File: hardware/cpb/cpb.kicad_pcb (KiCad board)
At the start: 6 copper layers, 95.9 x 90.2 mm, 238 parts, among them J1 Conn_02x20_Odd_Even, J10 SW1, J11 SW2, J12 SW3, J13 PISW1, J14 μSW1, J15 μSW2, J16 μSW3, J17 μSW4, J2 I2CExt, J3 DAC1BUF, J4 DAC2BUF, J6 Conn_02x20_Odd_Even, J7 ADC6/7, J8 ADC2/3, J9 4FBRG, J99 RBFJUMP, Q1 PMBT2222A, Q10 BSS138PS,115, Q11 BSS138PS,115, Q12 MBT2222ADW1T1, Q13 MBT2222ADW1T1, Q14 BSS138PS,115, Q15 BSS138PS,115, Q16 MBT2222ADW1T1, Q17 MBT2222ADW1T1, Q18 BSS138PS,115, Q19 BSS138PS,115, Q2 IRF9393, Q20 MBT2222ADW1T1, Q21 MBT2222ADW1T1, Q22 BSS138PS,115, Q23 BSS138PS,115, Q24 MBT2222ADW1T1, Q25 IRF7306, Q26 MBT2222ADW1T1, Q27 IRF7306, Q28 MBT2222ADW1T1, Q29 IRF7306, Q3 MBT2222ADW1T1, Q30 MBT2222ADW1T1, Q31 IRF7306, Q4 PMBT2222A, Q5 PMBT2222A, Q6 IRF9393, Q7 PMBT2222A, Q8 MBT2222ADW1T1, Q9 MBT2222ADW1T1, U1 TS912, U2 ADR420ARMZ, U3 KF33BDT, U4 STM32L072R_B-Z_Tx, U5 AP62301WU, U6 SC16IS750xBS, U7 SC18IS606, U8 KF33BDT, U9 MAX22200, Y1 14.7456MHz

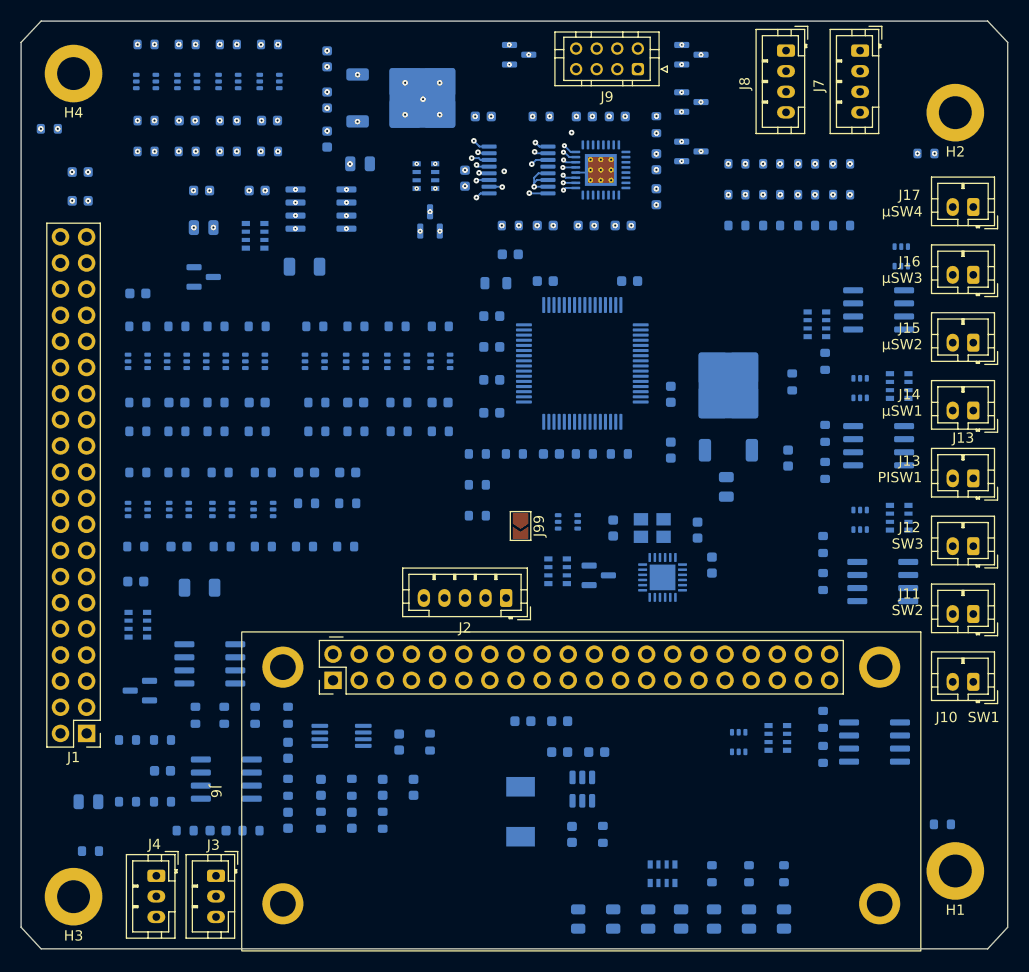
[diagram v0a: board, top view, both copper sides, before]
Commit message: cpb: continued work towards layout
- Adjust schematic; add datasheets, correct switcher output.  Additional
validation required.
- Adjust text.
- Add graphics
- Update design rules
- Perform an initial DRC in schematic & in layout.
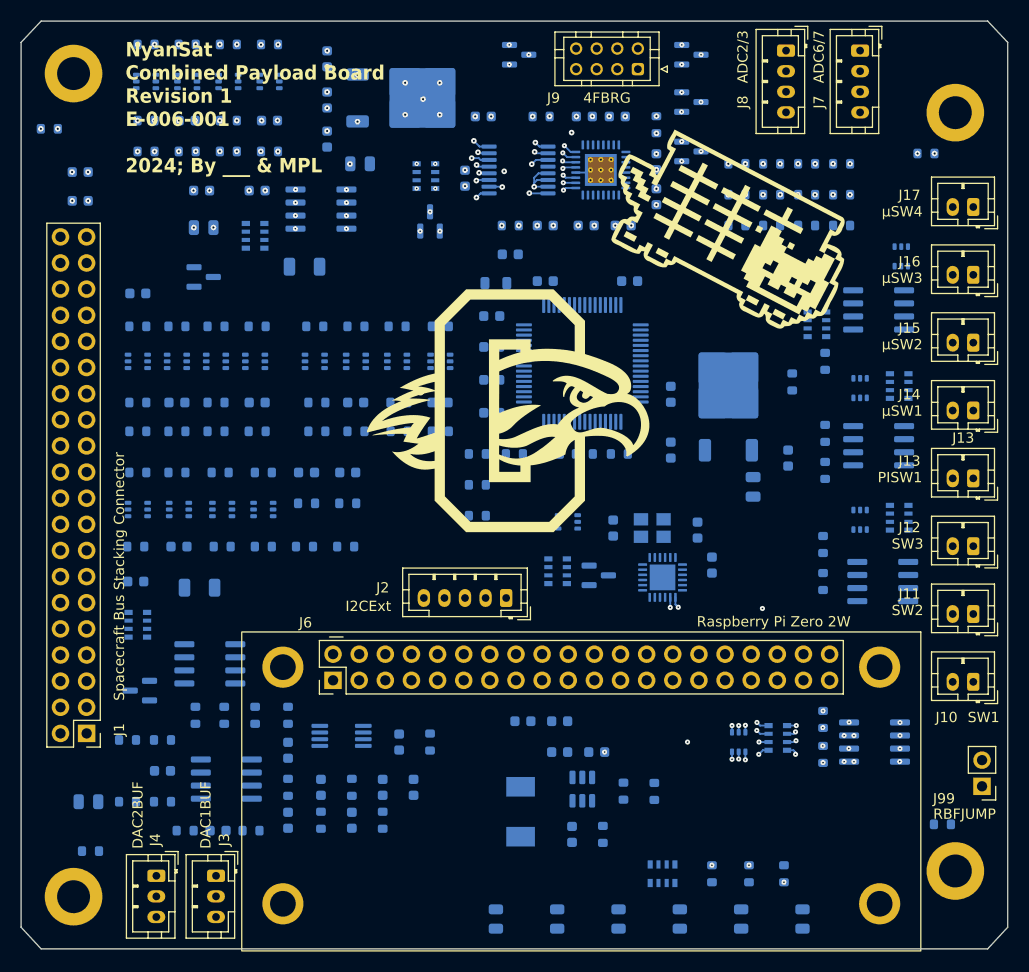
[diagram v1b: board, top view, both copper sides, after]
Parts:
- removed D4: PI3V3, LED_SMD:LED_0805_2012Metric
- added R44: 30k, Resistor_SMD:R_0603_1608Metric, B.Cu at (159.4, 133.1)
- added R45: 5.6k, Resistor_SMD:R_0603_1608Metric, B.Cu at (162.4, 133.1)
- J1: value Conn_02x20_Odd_Even -> Spacecraft Bus Stacking Connector
- J6: value Conn_02x20_Odd_Even -> Raspberry Pi Zero 2W
- J99: footprint Jumper:SolderJumper-2_P1.3mm_Open_TrianglePad1.0x1.5mm -> Connector_PinHeader_2.54mm:PinHeader_1x02_P2.54mm_Vertical
- moved J99 51.5 mm to (194.2, 132.6), turned to 180 degrees
- moved D7 8.00 mm to (147.0, 145.5)
- moved D6 5.44 mm to (153.0, 145.5)
- moved D3 3.32 mm to (164.9, 145.5)
- moved D5 2.88 mm to (158.9, 145.5)
- moved C8 2.60 mm to (172.0, 103.5)
- moved D1 1.80 mm to (176.8, 145.5)
- moved D2 0.76 mm to (170.8, 145.5)
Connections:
- RN2 pad 1: Net-(D4-A) -> (no net)
- RN2 pad 8: /PI3V3 -> (no net)
- U5 pad 4: +5V -> Net-(U5-FB)
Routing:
- net /SW2: track 0.00 -> 22.6 mm, vias 0 -> 3
- net /SW1: track 0.00 -> 21.9 mm, vias 0 -> 3
- net /PairPowerSwitches1/OUT2: track 0.00 -> 14.7 mm, vias 0 -> 2
- net Net-(Q24A-C1): track 0.00 -> 13.0 mm, vias 0 -> 3
- net Net-(Q24B-C2): track 0.00 -> 11.8 mm, vias 0 -> 3
- net /PairPowerSwitches1/OUT1: track 0.00 -> 11.6 mm, vias 0 -> 2
- net Net-(Q24B-B2): track 0.00 -> 10.2 mm, vias 0 -> 3
- net Net-(Q24A-B1): track 0.00 -> 9.43 mm, vias 0 -> 3
- net GND: track 10.4 -> 14.2 mm, vias 34 -> 38
- net +7.5V: track 0.00 -> 0.10 mm, vias 0 -> 8
- net +3.3V: track 0.00 -> 0.03 mm, vias 2 -> 3
- net +5V: vias 0 -> 1
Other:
- board text added: "NyanSat Combined Payload Board Revision 1 E-006-001 2024; By ___ & MPL"

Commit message: hardware/cpb: continuing of board layout
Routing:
- net GND: track 14.2 -> 28.9 mm, vias 38 -> 69
- net /FourFullBridges/VM: track 0.00 -> 8.35 mm, vias 12 -> 20
- net /SDA: track 0.00 -> 4.75 mm, vias 0 -> 6
- net /SCL: track 0.00 -> 3.11 mm, vias 0 -> 4
- net /UARTSDA: track 0.00 -> 2.11 mm, vias 0 -> 4
- net Net-(Q13B-B2): track 0.00 -> 2.09 mm, vias 0 -> 4
- net Net-(Q17B-B2): track 0.00 -> 1.84 mm, vias 0 -> 4
- net /uSDA: track 0.00 -> 1.82 mm, vias 0 -> 4
- net Net-(Q12B-B2): track 0.00 -> 1.69 mm, vias 0 -> 4
- net /FourFullBridges/FBRDG3V3: track 2.21 -> 3.87 mm, vias 16 -> 18
- net Net-(Q16B-B2): track 0.00 -> 1.61 mm, vias 0 -> 4
- net Net-(Q18A-G2): track 0.00 -> 1.54 mm, vias 0 -> 3
- net Net-(Q15A-G2): track 0.00 -> 1.47 mm, vias 0 -> 3
- net Net-(Q5-B): track 0.00 -> 1.47 mm, vias 0 -> 4
- net /FourFullBridges/FBRGEN: track 0.00 -> 1.43 mm, vias 1 -> 3
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
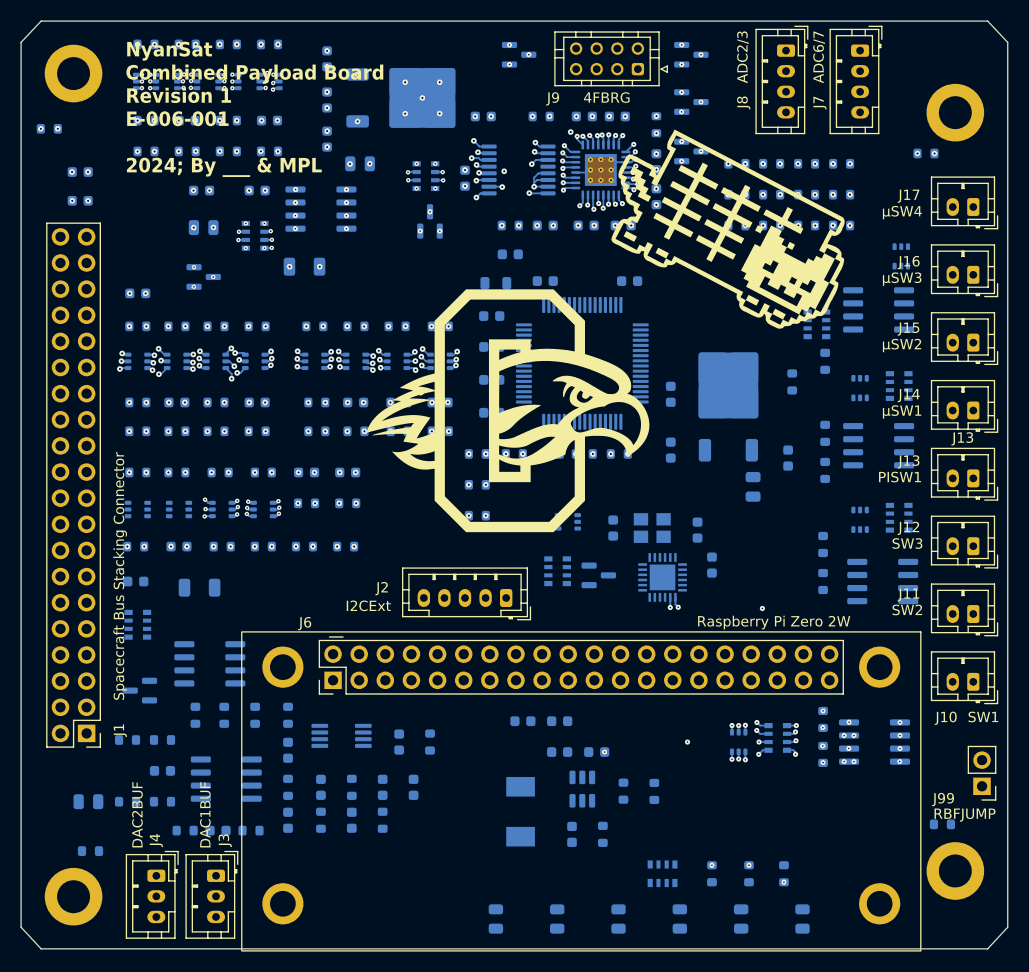
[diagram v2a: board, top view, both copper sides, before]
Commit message: hardware/cpb: Further cpb layout
Finished placing all vias and beginning of routing.
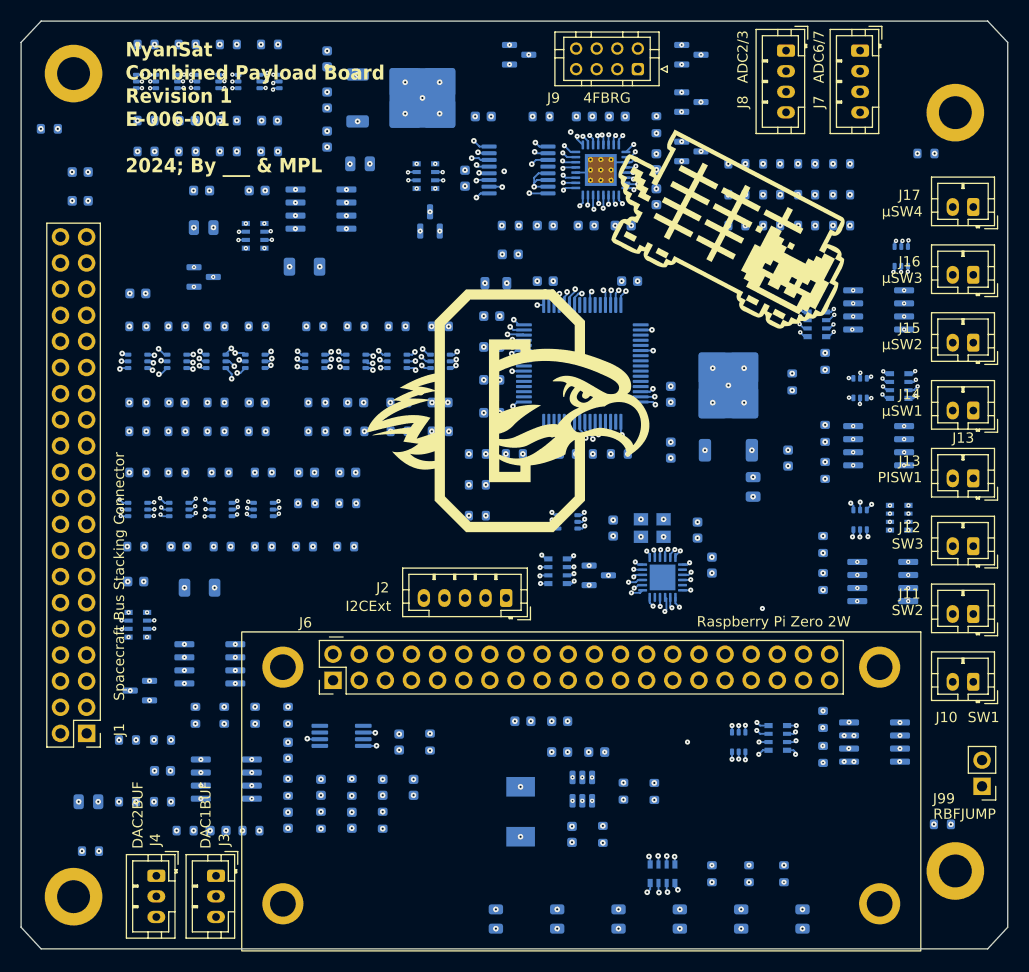
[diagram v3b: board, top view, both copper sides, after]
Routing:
- net GND: track 28.9 -> 51.2 mm, vias 69 -> 141
- net +3.3V: track 0.03 -> 11.1 mm, vias 31 -> 50
- net Net-(Q3A-C1): track 0.00 -> 3.23 mm, vias 0 -> 4
- net /uSW2: track 0.00 -> 2.82 mm, vias 0 -> 2
- net /~{MICRORST}: track 0.00 -> 2.66 mm, vias 0 -> 5
- net /uSW3: track 0.00 -> 2.62 mm, vias 0 -> 2
- net /uSW1: track 0.00 -> 2.50 mm, vias 0 -> 2
- net Net-(Q30A-B1): track 0.00 -> 2.49 mm, vias 0 -> 3
- net Net-(Q28B-B2): track 0.00 -> 2.46 mm, vias 0 -> 3
- net Net-(Q30B-B2): track 0.00 -> 2.38 mm, vias 0 -> 3
- net Net-(Q28A-B1): track 0.00 -> 2.11 mm, vias 0 -> 3
- net /TIM3_CH2: track 0.00 -> 2.06 mm, vias 0 -> 2
- net /uSW4: track 0.00 -> 2.05 mm, vias 0 -> 2
- net /GPLED: track 0.00 -> 1.81 mm, vias 0 -> 2
- net /ADC6: track 0.00 -> 1.77 mm, vias 3 -> 4
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
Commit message: cpb: routing in progress
- Adjust layout for easier routing.
- Pin swap clamping diodes to simplify routing.
- Route the high power nets
- Adjust plane pours.
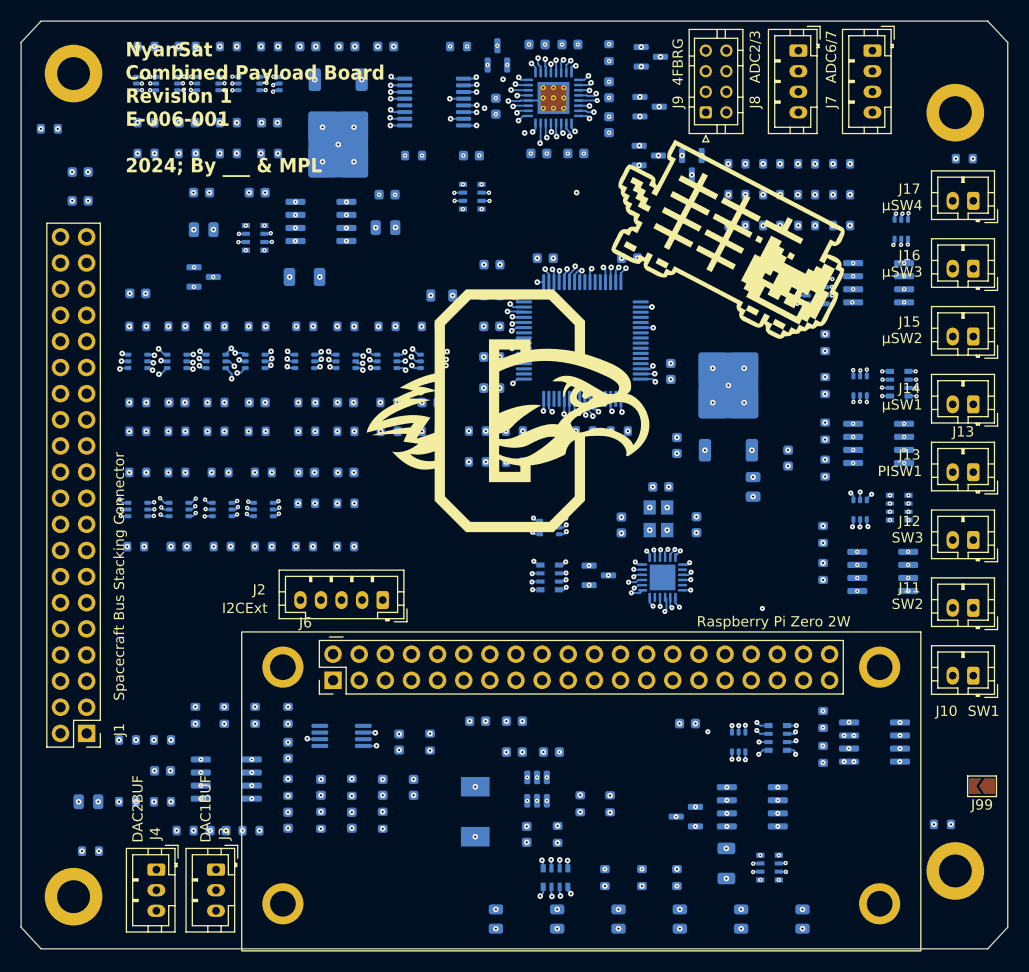
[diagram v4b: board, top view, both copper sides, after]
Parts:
- J99: footprint Connector_PinHeader_2.54mm:PinHeader_1x02_P2.54mm_Vertical -> Jumper:SolderJumper-2_P1.3mm_Open_TrianglePad1.0x1.5mm
- moved RN1 65.8 mm to (173.6, 140.5), turned to 180 degrees
- moved R1 57.8 mm to (169.4, 140.1), turned to 90 degrees
- moved C5 55.4 mm to (165.6, 126.5)
- moved Q2 54.5 mm to (171.9, 134.6)
- moved Q1 54.5 mm to (165.5, 135.6)
- moved R51 18.1 mm to (143.4, 60.7), turned to 0 degrees
- moved Q7 17.4 mm to (147.2, 61.6)
- moved C43 15.7 mm to (136.4, 75.1), turned to 0 degrees
- moved R49 13.0 mm to (139.0, 71.3), turned to 180 degrees
- moved D11 12.8 mm to (162.1, 61.7)
- moved J2 12.0 mm to (136.0, 114.5)
- moved D8 10.7 mm to (166.1, 72.2), turned to -90 degrees
- moved U7 10.5 mm to (141.0, 66.1), turned to 0 degrees
- moved R22 10.4 mm to (164.6, 141.5)
- moved R23 10.4 mm to (161.2, 141.5)
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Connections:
- D11 pad 1: /FourFullBridges/OUT4A -> /FourFullBridges/OUT4B
- D11 pad 2: /FourFullBridges/OUT4B -> /FourFullBridges/OUT4A
- Q8 pad 1: /FBSCL -> /SCL
- Q8 pad 3: /FBSCL -> /SCL
- Q9 pad 1: /FBSDA -> /SDA
- Q9 pad 3: /FBSDA -> /SDA
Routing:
- net /FourFullBridges/FBRGEN: track 1.43 -> 33.4 mm, vias 3 -> 4
- net /FourFullBridges/OUT1B: track 1.41 -> 28.8 mm
- net /FourFullBridges/OUT1A: track 0.98 -> 23.9 mm
- net /FourFullBridges/OUT3B: track 1.05 -> 23.5 mm
- net /FourFullBridges/OUT3A: track 1.05 -> 22.4 mm
- net /FourFullBridges/~{REQFBRGEN}: track 1.82 -> 23.0 mm
- net /FourFullBridges/OUT2A: track 0.89 -> 20.0 mm
- net /FourFullBridges/OUT2B: track 0.96 -> 19.2 mm
- net /FourFullBridges/OUT4B: track 0.99 -> 18.0 mm
- net /FourFullBridges/OUT4A: track 0.99 -> 17.6 mm
- net /PairPowerSwitches3/OUT2: track 0.00 -> 14.7 mm
- net /PairPowerSwitches2/OUT2: track 0.00 -> 12.9 mm
- net /PairPowerSwitches4/OUT2: track 0.00 -> 12.2 mm
- net /PairPowerSwitches3/OUT1: track 0.00 -> 11.6 mm
- net Net-(RN8D-R4.1): track 1.28 -> 11.2 mm
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
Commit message: hardware/cpb: began routing 240 remaining
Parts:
- moved R43 0.98 mm to (104.5, 68.5), turned to 180 degrees
- turned R82 to 0 degrees
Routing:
- net Net-(Q30B-C2): track 0.63 -> 47.3 mm, vias 3 -> 12
- net Net-(Q30A-B1): track 1.99 -> 19.5 mm, vias 3 -> 7
- net Net-(Q28B-C2): track 0.62 -> 13.9 mm, vias 3 -> 5
- net Net-(Q11A-D1): track 1.36 -> 11.6 mm, vias 4 -> 7
- net Net-(Q10A-D1): track 1.19 -> 11.4 mm, vias 4 -> 5
- net Net-(J7-Pin_4): track 0.00 -> 10.1 mm, vias 1 -> 2
- net Net-(Q28A-C1): track 0.62 -> 10.7 mm, vias 3 -> 7
- net Net-(J7-Pin_2): track 0.00 -> 9.90 mm
- net Net-(Q10B-G1): track 0.55 -> 10.4 mm, vias 3 -> 5
- net Net-(J8-Pin_2): track 0.00 -> 9.74 mm
- net Net-(J1-Pin_37): track 0.00 -> 8.90 mm
- net Net-(J8-Pin_4): track 0.00 -> 8.88 mm
- net /FourFullBridges/PCVTSCL: track 2.55 -> 10.7 mm, vias 5 -> 6
- net Net-(Q11B-G1): track 0.68 -> 8.49 mm
- net Net-(Q28B-B2): track 2.16 -> 8.69 mm
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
